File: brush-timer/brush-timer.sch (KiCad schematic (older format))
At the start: 13 parts, among them Q1 BC327, Q2 BC337, SW1 Power, U1 Arduino_Pro_Mini

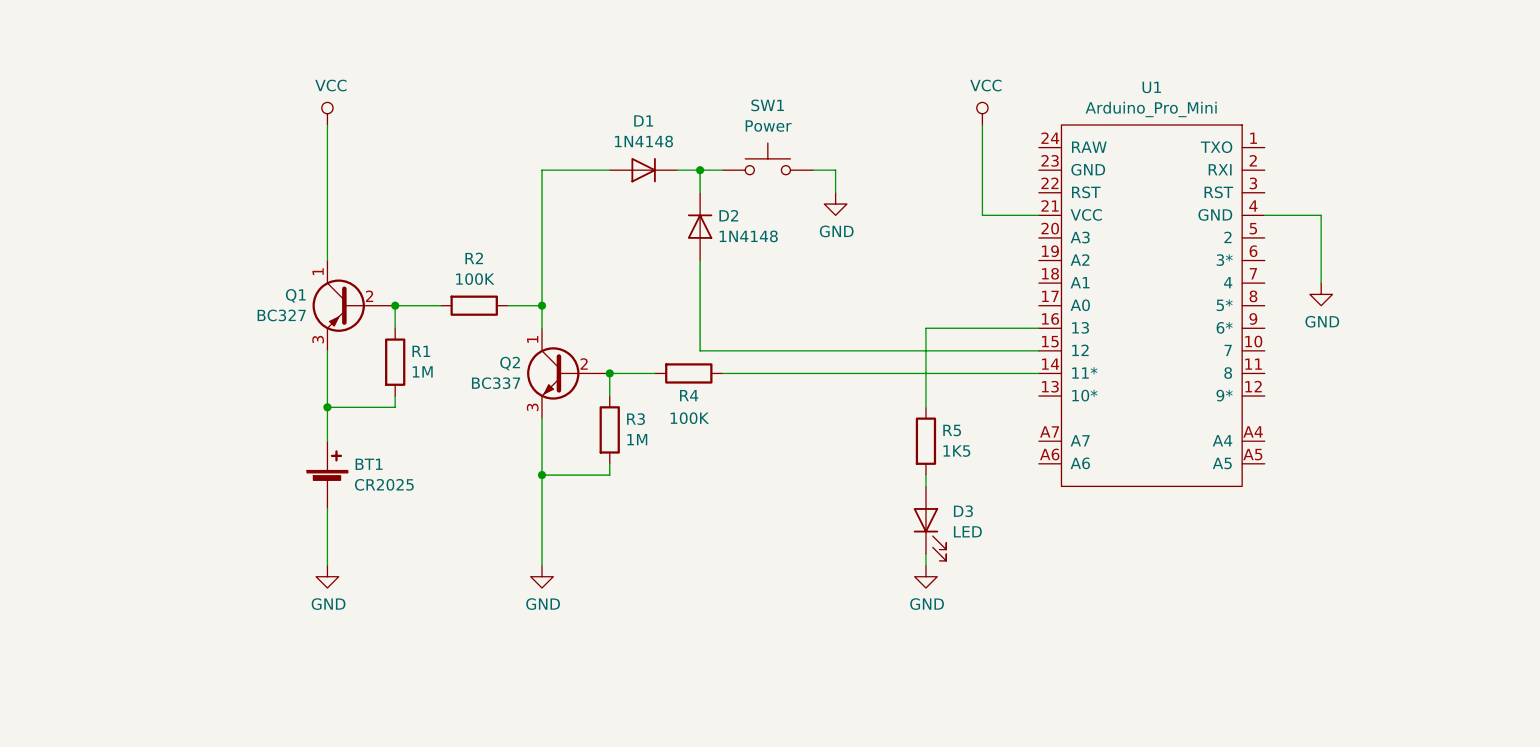
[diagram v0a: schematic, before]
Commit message: Updated brush-timer.sh
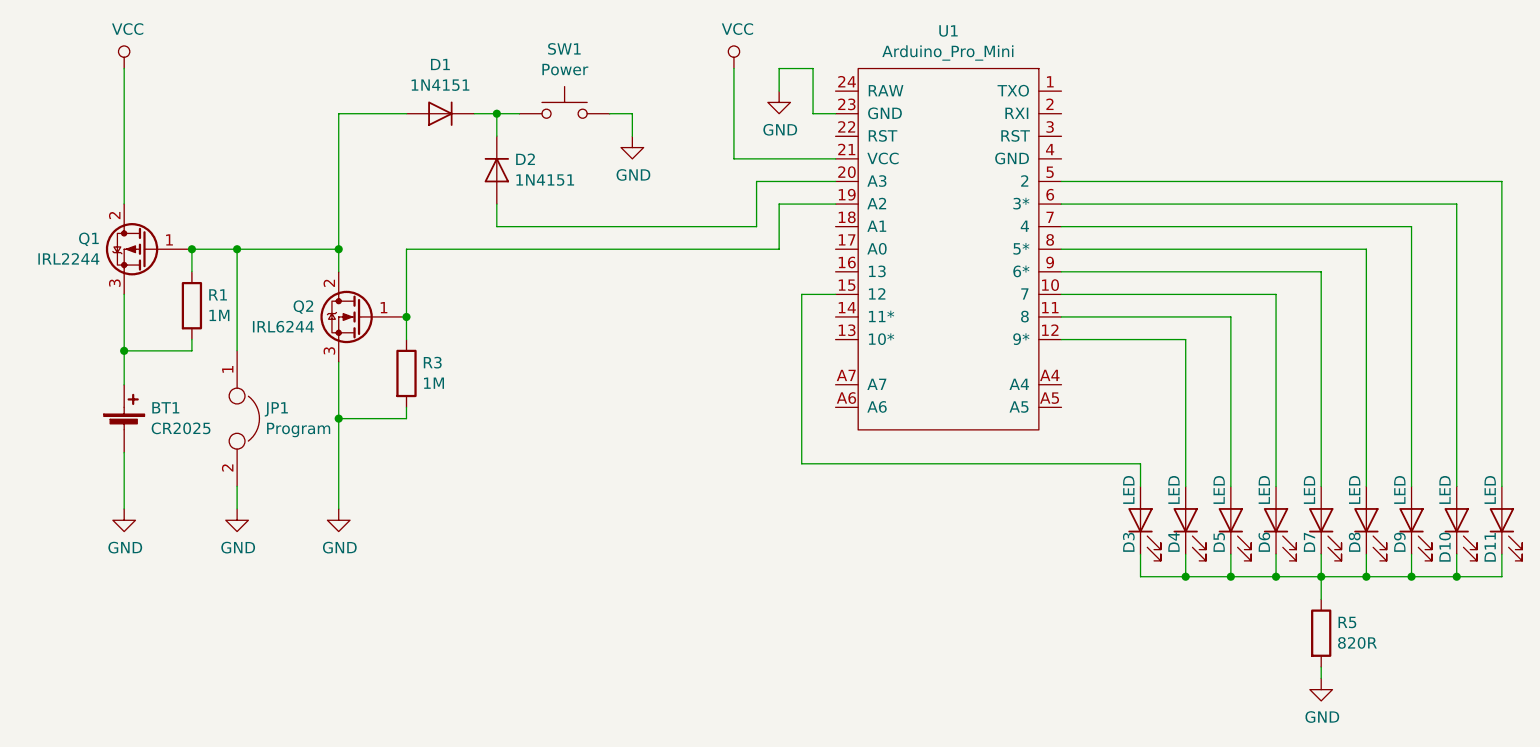
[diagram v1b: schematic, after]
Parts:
- removed Q1: BC327, symbol Device:Q_PNP_CBE
- removed Q2: BC337, symbol Device:Q_NPN_CBE
- removed R2, R4: 100K, symbol Device:R
- added D10, D11, D4, D5, D6, D7, D8, D9: LED, symbol Device:LED
- added JP1: Program, symbol Device:Jumper
- added Q1: IRL2244, symbol Device:Q_PMOS_GDS
- added Q2: IRL6244, symbol Device:Q_NMOS_GDS
- D1, D2: value 1N4148 -> 1N4151
- R5: value 1K5 -> 820R
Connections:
- net GND: now also R5.2, U1.23 (GND), JP1.2, Q2.3 (S); no longer D3.1 (K), U1.4 (GND)
- net VCC: now also Q1.2 (D)
- net at R1.1: now also D1.2 (A), JP1.1, Q1.1 (G), Q2.2 (D)
- net at BT1.1 (+), R1.2: now also Q1.3 (S)
- net at R3.1: now also U1.19 (A2), Q2.1 (G)
- net at U1.10 (7): now also D6.2 (A)
- net at U1.11 (8): now also D5.2 (A)
- net at U1.12 (9*): now also D4.2 (A)
- net at U1.15 (12): now also D3.2 (A); no longer D2.2 (A)
- net at U1.16 (13): no longer R5.1
- net at U1.20 (A3): now also D2.2 (A)
- net at U1.5 (2): now also D11.2 (A)
- net at U1.6 (3*): now also D10.2 (A)
- net at U1.7 (4): now also D9.2 (A)
- net at U1.8 (5*): now also D8.2 (A)
- net at U1.9 (6*): now also D7.2 (A)
- new net: D10.1 (K), D11.1 (K), D3.1 (K), D4.1 (K), D5.1 (K), D6.1 (K), D7.1 (K), D8.1 (K), D9.1 (K), R5.1
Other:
- moved on the sheet: BT1, D1, D2, D3, R1, R3, R5, SW1, U1
